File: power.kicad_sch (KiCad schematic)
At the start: 63 parts, among them J3 Conn_02x05_Odd_Even, T1 net-tie, U1 LMR54410, U2 RT9080-33GJ5, U3 TPS546D24ARVFR, U4 MIC5504

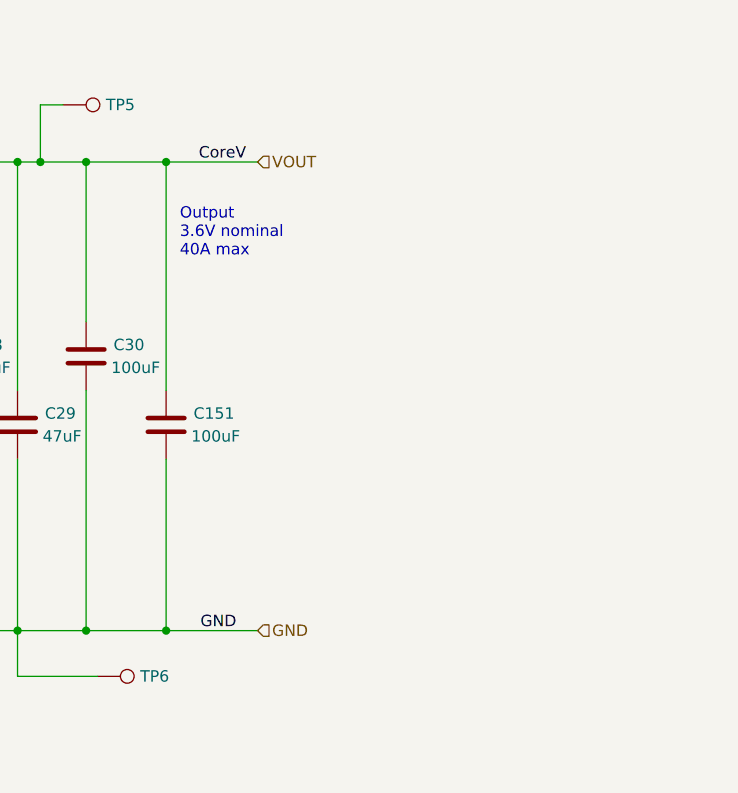
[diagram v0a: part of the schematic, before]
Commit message: add v304 fix to schematic
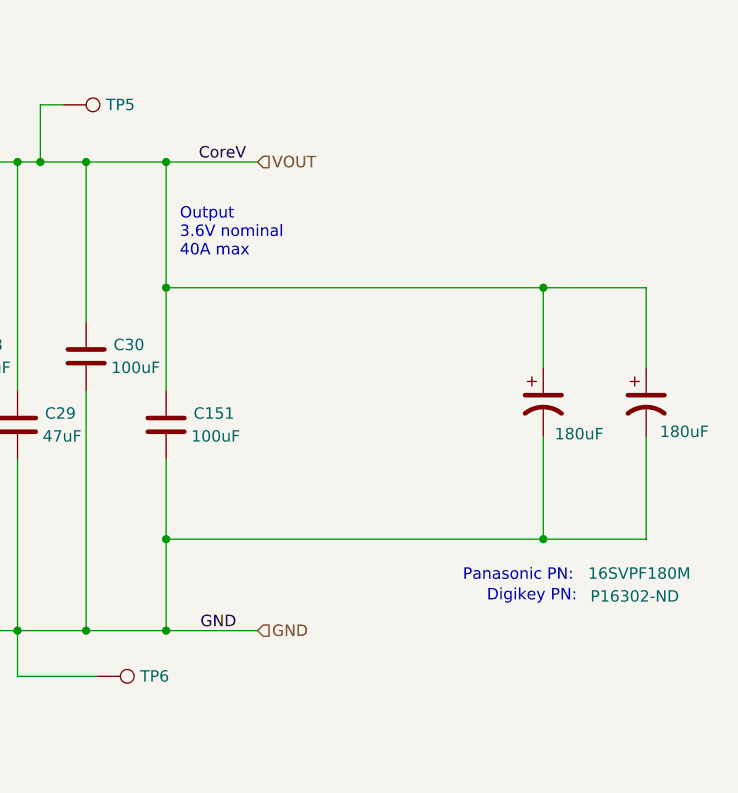
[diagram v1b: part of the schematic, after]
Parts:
- added C155, C156: 180uF, symbol Device:C_Polarized_US
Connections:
- net GND: now also C155.2, C156.2
- net VOUT: now also C155.1, C156.1
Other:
- note added: "Digikey PN:"
- note added: "Panasonic PN:"
